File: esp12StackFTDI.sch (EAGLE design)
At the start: 23 parts, among them J02 470, J04 470, J05 470, J12 470, J13 470

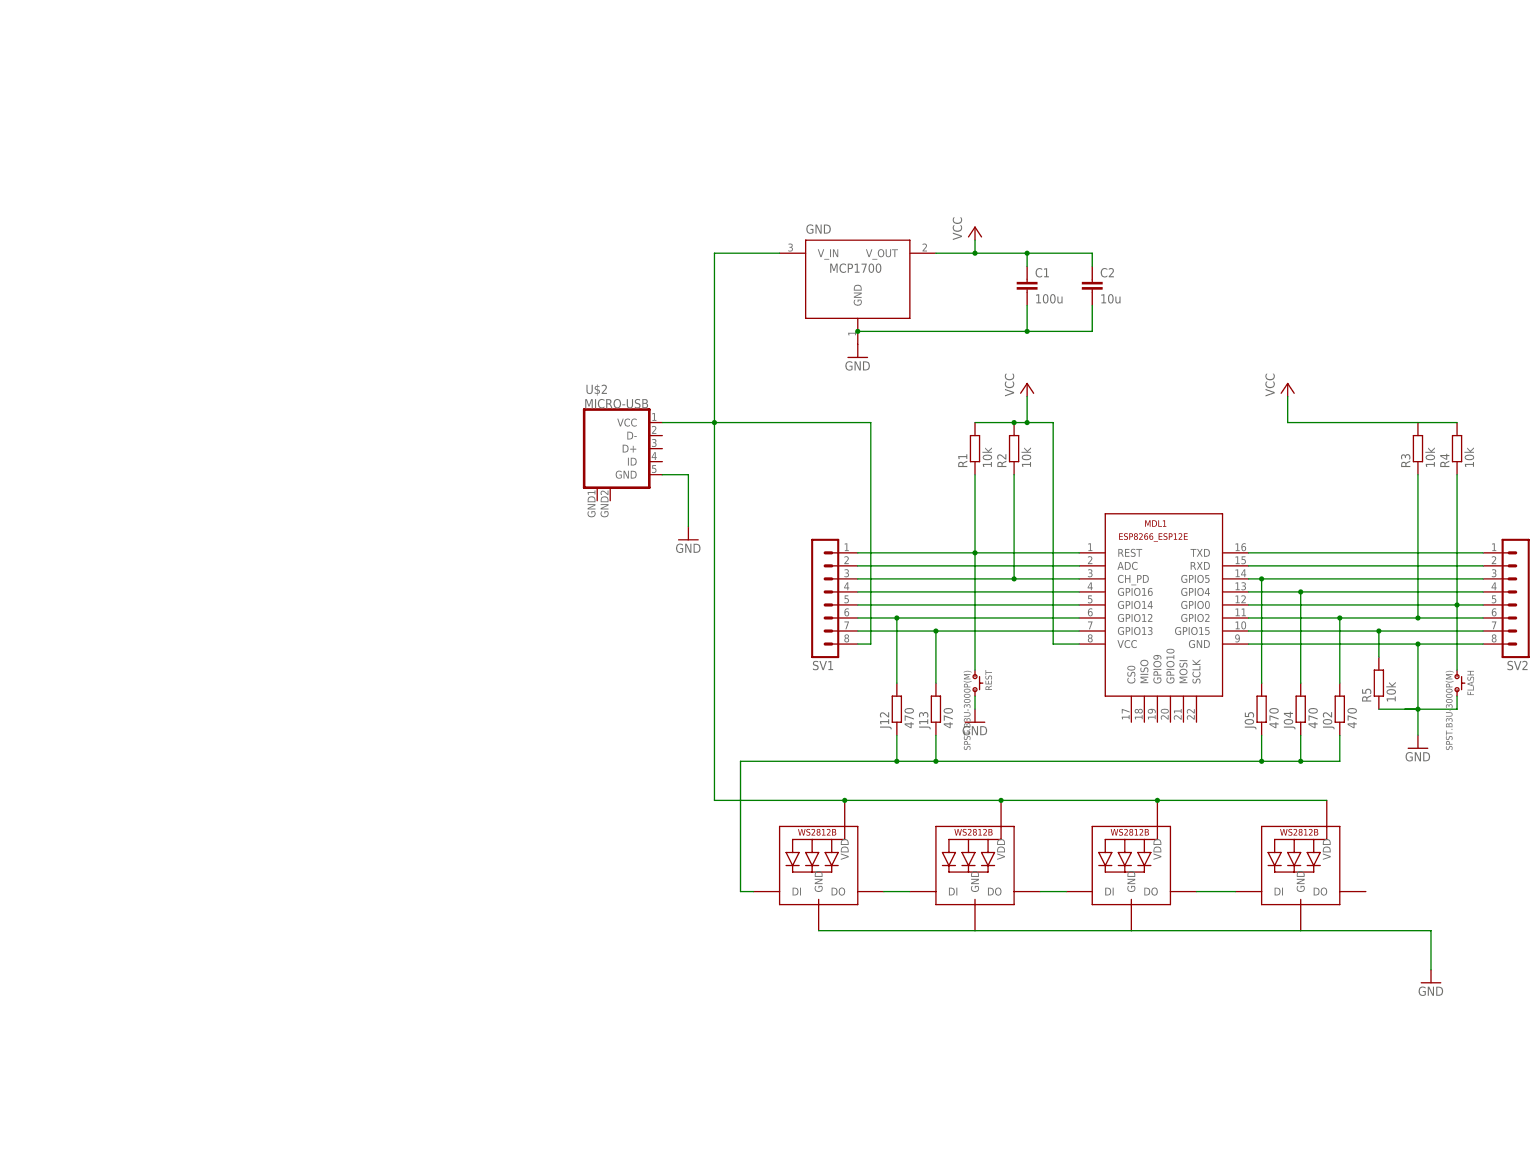
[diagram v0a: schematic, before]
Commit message: added an ftdi version
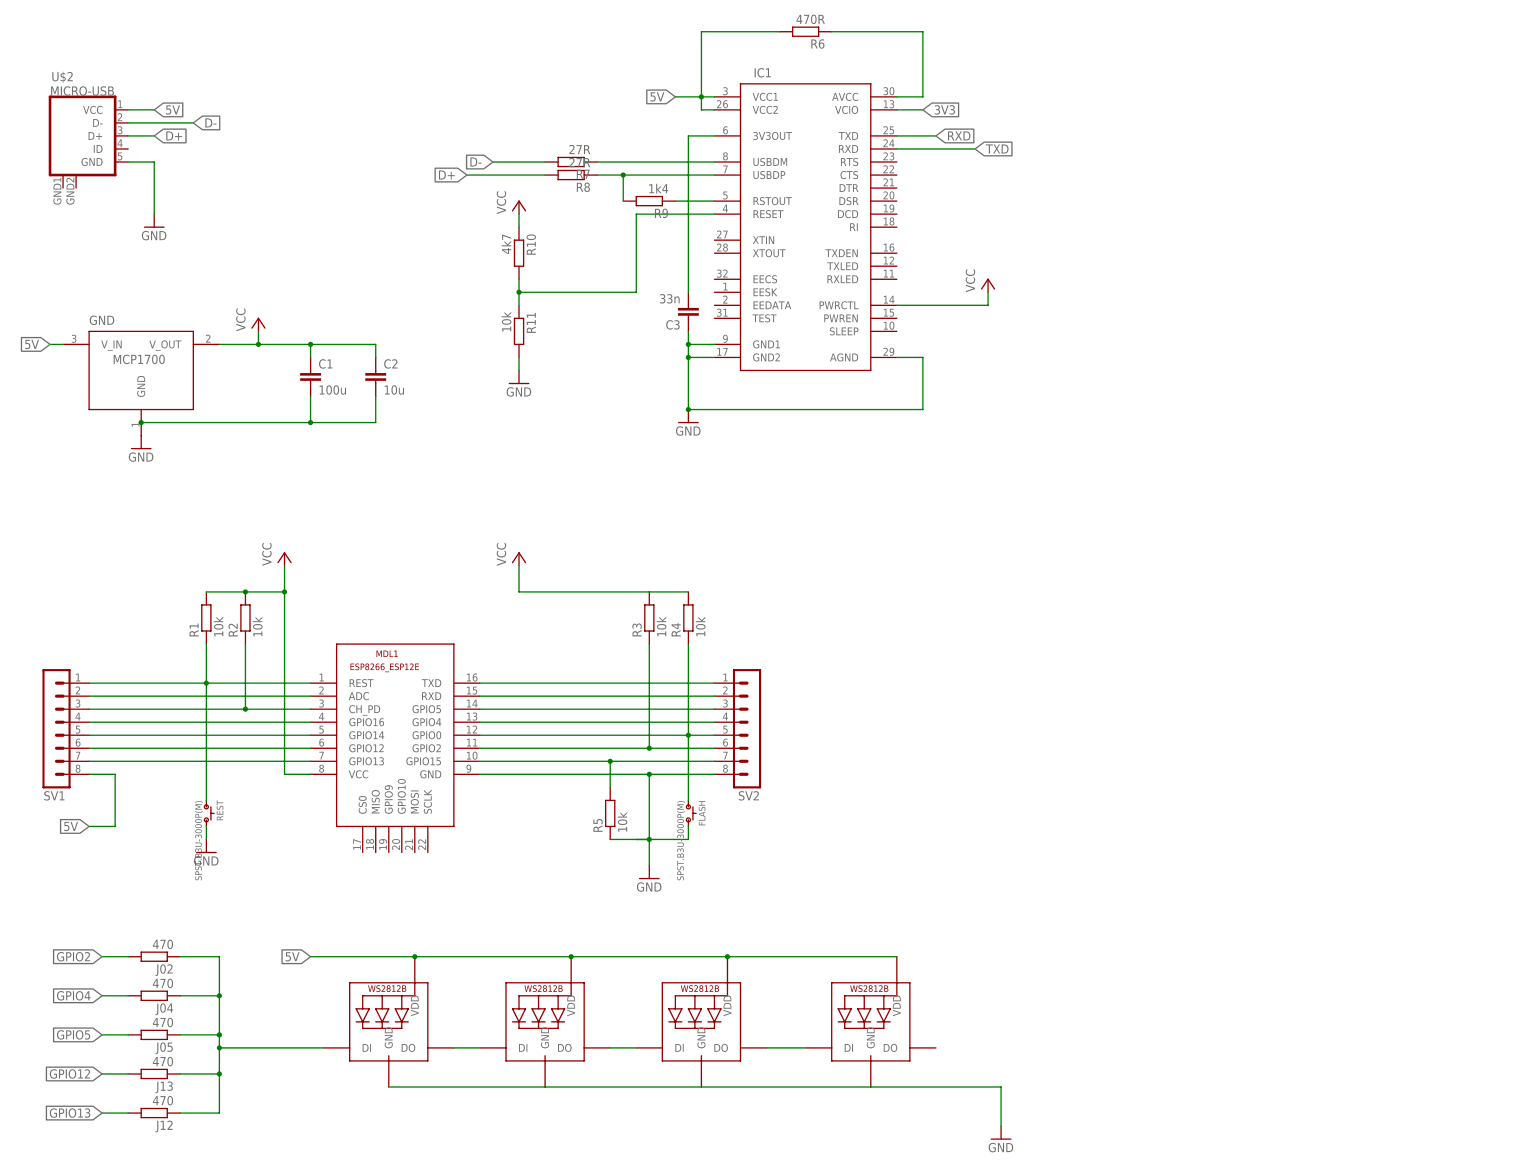
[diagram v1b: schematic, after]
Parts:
- added C3: 33n, eagle-ltspice:CC0603
- added IC1: (no value), FTDI:FT232BM
- added R10: 4k7, eagle-ltspice:RR0603
- added R11: 10k, eagle-ltspice:RR0603
- added R6: 470R, eagle-ltspice:RR0603
- added R7, R8: 27R, eagle-ltspice:RR0603
- added R9: 1k4, eagle-ltspice:RR0603
- J02, J04, J05, J12, J13, R1, R2, R3, R4, R5: device eagle-ltspice:R -> eagle-ltspice:RR0603
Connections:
- net DIN renamed DIN1
- new net 3V3OUT: C3.2, IC1.3V3OUT
- new net AVCC: IC1.AVCC, R6.1
- new net D+: R8.2, U$2.D+
- new net D-: R7.2, U$2.D-
- new net RESET: IC1.RESET, R10.2, R11.1
- new net RSTOUT: IC1.RSTOUT, R9.1
- new net USBDM: IC1.USBDM, R7.1
- new net USBDP: IC1.USBDP, R8.1, R9.2
- net 3V3: now also IC1.PWRCTL, IC1.VCIO
- net 5V: now also IC1.VCC1, IC1.VCC2, R10.1, R6.2
- net GND: now also C3.1, IC1.AGND, IC1.GND1, IC1.GND2, R11.2
- net GPIO12: now also J13.2; no longer J12.2
- net GPIO13: now also J12.2; no longer J13.2
- net RXD: now also IC1.TXD
- net TXD: now also IC1.RXD
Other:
- moved on the sheet: C1, C2, FLASH, GND, J02, J04, J05, J12, J13, MDL1, R1, R2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

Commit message: Deep Sleep capability
added a jumper Position to connect GIPO16 and REST to enable wake up from deep sleep.
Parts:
- added J_REST: 10k, eagle-ltspice:RR0603
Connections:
- net GPIO16: now also J_REST.1
- net REST: now also J_REST.2
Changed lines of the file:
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@@
 <grid distance="0.1" unitdist="inch" unit="inch" style="lines" multiple="1" display="no" altdistance="0.01" altunitdist="inch" altunit="inch"/>
 <layers>
-<layer number="1" name="Top" color="4" fill="1" visible="yes" active="no"/>
-<layer number="16" name="Bottom" color="1" fill="1" visible="yes" active="no"/>
-<layer number="17" name="Pads" color="2" fill="1" visible="yes" active="no"/>
-<layer number="18" name="Vias" color="2" fill="1" visible="yes" active="no"/>
-<layer number="19" name="Unrouted" color="6" fill="1" visible="yes" active="no"/>
-<layer number="20" name="Dimension" color="15" fill="1" visible="yes" active="no"/>
-<layer number="21" name="tPlace" color="7" fill="1" visible="yes" active="no"/>
-<layer number="22" name="bPlace" color="7" fill="1" visible="yes" active="no"/>
-<layer number="23" name="tOrigins" color="15" fill="1" visible="yes" active="no"/>
-<layer number="24" name="bOrigins" color="15" fill="1" visible="yes" active="no"/>
-<layer number="25" name="tNames" color="7" fill="1" visible="yes" active="no"/>
-<layer number="26" name="bNames" color="7" fill="1" visible="yes" active="no"/>
-<layer number="27" name="tValues" color="7" fill="1" visible="yes" active="no"/>
-<layer number="28" name="bValues" color="7" fill="1" visible="yes" active="no"/>
+<layer number="1" name="Top" color="4" fill="1" visible="no" active="no"/>
+<layer number="16" name="Bottom" color="1" fill="1" visible="no" active="no"/>
+<layer number="17" name="Pads" color="2" fill="1" visible="no" active="no"/>
+<layer number="18" name="Vias" color="2" fill="1" visible="no" active="no"/>
+<layer number="19" name="Unrouted" color="6" fill="1" visible="no" active="no"/>
+<layer number="20" name="Dimension" color="15" fill="1" visible="no" active="no"/>
+<layer number="21" name="tPlace" color="7" fill="1" visible="no" active="no"/>
+<layer number="22" name="bPlace" color="7" fill="1" visible="no" active="no"/>
+<layer number="23" name="tOrigins" color="15" fill="1" visible="no" active="no"/>
+<layer number="24" name="bOrigins" color="15" fill="1" visible="no" active="no"/>
+<layer number="25" name="tNames" color="7" fill="1" visible="no" active="no"/>
+<layer number="26" name="bNames" color="7" fill="1" visible="no" active="no"/>
+<layer number="27" name="tValues" color="7" fill="1" visible="no" active="no"/>
+<layer number="28" name="bValues" color="7" fill="1" visible="no" active="no"/>
 <layer number="29" name="tStop" color="7" fill="3" visible="no" active="no"/>
 <layer number="30" name="bStop" color="7" fill="6" visible="no" active="no"/>
@@
 <layer number="35" name="tGlue" color="7" fill="4" visible="no" active="no"/>
 <layer number="36" name="bGlue" color="7" fill="5" visible="no" active="no"/>
-<layer number="37" name="tTest" color="7" fill="1" visible="yes" active="no"/>
-<layer number="38" name="bTest" color="7" fill="1" visible="yes" active="no"/>
+<layer number="37" name="tTest" color="7" fill="1" visible="no" active="no"/>
+<layer number="38" name="bTest" color="7" fill="1" visible="no" active="no"/>
 <layer number="39" name="tKeepout" color="4" fill="11" visible="no" active="no"/>
 <layer number="40" name="bKeepout" color="1" fill="11" visible="no" active="no"/>
@@
 <layer number="44" name="Drills" color="7" fill="1" visible="no" active="no"/>
 <layer number="45" name="Holes" color="7" fill="1" visible="no" active="no"/>
-<layer number="46" name="Milling" color="3" fill="1" visible="yes" active="no"/>
-<layer number="47" name="Measures" color="7" fill="1" visible="yes" active="no"/>
-<layer number="48" name="Document" color="7" fill="1" visible="yes" active="no"/>
-<layer number="49" name="Reference" color="7" fill="1" visible="yes" active="no"/>
-<layer number="50" name="dxf" color="7" fill="1" visible="yes" active="no"/>
-<layer number="51" name="tDocu" color="7" fill="1" visible="yes" active="no"/>
-<layer number="52" name="bDocu" color="7" fill="1" visible="yes" active="no"/>
-<layer number="53" name="tGND_GNDA" color="7" fill="9" visible="yes" active="no"/>
-<layer number="54" name="bGND_GNDA" color="1" fill="9" visible="yes" active="no"/>
-<layer number="56" name="wert" color="7" fill="1" visible="yes" active="no"/>
-<layer number="57" name="tCAD" color="7" fill="1" visible="yes" active="no"/>
-<layer number="59" name="tCarbon" color="7" fill="1" visible="yes" active="no"/>
-<layer number="60" name="bCarbon" color="7" fill="1" visible="yes" active="no"/>
+<layer number="46" name="Milling" color="3" fill="1" visible="no" active="no"/>
+<layer number="47" name="Measures" color="7" fill="1" visible="no" active="no"/>
+<layer number="48" name="Document" color="7" fill="1" visible="no" active="no"/>
+<layer number="49" name="Reference" color="7" fill="1" visible="no" active="no"/>
+<layer number="50" name="dxf" color="7" fill="1" visible="no" active="no"/>
+<layer number="51" name="tDocu" color="7" fill="1" visible="no" active="no"/>
+<layer number="52" name="bDocu" color="7" fill="1" visible="no" active="no"/>
+<layer number="53" name="tGND_GNDA" color="7" fill="9" visible="no" active="no"/>
+<layer number="54" name="bGND_GNDA" color="1" fill="9" visible="no" active="no"/>
+<layer number="56" name="wert" color="7" fill="1" visible="no" active="no"/>
+<layer number="57" name="tCAD" color="7" fill="1" visible="no" active="no"/>
+<layer number="59" name="tCarbon" color="7" fill="1" visible="no" active="no"/>
+<layer number="60" name="bCarbon" color="7" fill="1" visible="no" active="no"/>
 <layer number="90" name="Modules" color="5" fill="1" visible="yes" active="yes"/>
 <layer number="91" name="Nets" color="2" fill="1" visible="yes" active="yes"/>
@@
 <part name="P+2" library="supply1" deviceset="VCC" device=""/>
 <part name="P+5" library="supply1" deviceset="VCC" device=""/>
+<part name="J_REST" library="eagle-ltspice" deviceset="R" device="R0603" value="10k"/>
 </parts>
 <sheets>
@@
 <instance part="P+2" gate="VCC" x="-35.56" y="111.76"/>
 <instance part="P+5" gate="VCC" x="55.88" y="96.52"/>
+<instance part="J_REST" gate="G$1" x="-111.76" y="30.48" rot="R90"/>
 </instances>
 <busses>
@@
 <wire x1="-76.2" y1="17.78" x2="-96.52" y2="17.78" width="0.1524" layer="91"/>
 <pinref part="R1" gate="G$1" pin="1"/>
-<wire x1="-96.52" y1="17.78" x2="-119.38" y2="17.78" width="0.1524" layer="91"/>
+<wire x1="-96.52" y1="17.78" x2="-106.68" y2="17.78" width="0.1524" layer="91"/>
+<wire x1="-106.68" y1="17.78" x2="-119.38" y2="17.78" width="0.1524" layer="91"/>
 <wire x1="-96.52" y1="25.4" x2="-96.52" y2="17.78" width="0.1524" layer="91"/>
 <junction x="-96.52" y="17.78"/>
 <wire x1="-96.52" y1="17.78" x2="-96.52" y2="-5.08" width="0.1524" layer="91"/>
 <pinref part="REST" gate="G$1" pin="1"/>
+<pinref part="J_REST" gate="G$1" pin="2"/>
+<wire x1="-111.76" y1="35.56" x2="-106.68" y2="35.56" width="0.1524" layer="91"/>
+<wire x1="-106.68" y1="35.56" x2="-106.68" y2="17.78" width="0.1524" layer="91"/>
+<junction x="-106.68" y="17.78"/>
 </segment>
 </net>
@@
 <pinref part="MDL1" gate="G$1" pin="GPIO16"/>
 <pinref part="SV1" gate="1" pin="4"/>
-<wire x1="-76.2" y1="10.16" x2="-119.38" y2="10.16" width="0.1524" layer="91"/>
+<wire x1="-76.2" y1="10.16" x2="-111.76" y2="10.16" width="0.1524" layer="91"/>
+<pinref part="J_REST" gate="G$1" pin="1"/>
+<wire x1="-111.76" y1="10.16" x2="-119.38" y2="10.16" width="0.1524" layer="91"/>
+<wire x1="-111.76" y1="10.16" x2="-111.76" y2="25.4" width="0.1524" layer="91"/>
+<junction x="-111.76" y="10.16"/>
 </segment>
 </net>

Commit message: FT232 module
FT232 Module now functional as a prototype
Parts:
- removed C3: 33n, eagle-ltspice:CC0603
- removed IC1: (no value), FTDI:FT232BM
- removed R8: 27R, eagle-ltspice:RR0603
- removed R9: 1k4, eagle-ltspice:RR0603
- added C4: 10nF, eagle-ltspice:C
- added C5: 100nF, eagle-ltspice:C
- added D1: (no value), adafruit:DIODESOD-323F
- added LED5, LED6: (no value), adafruit:LEDCHIPLED_0603
- added SJ2: SOLDERJUMPERNC2, SparkFun:SOLDERJUMPERNC2
- added U1: (no value), ftdichip-4:FT232RL
- R6: value 470R -> (none); device eagle-ltspice:RR0603 -> rcl:R-EU_R0603
- R7: value 27R -> (none); device eagle-ltspice:RR0603 -> rcl:R-EU_R0603
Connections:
- removed net AVCC: IC1.AVCC, R6.1
- removed net RSTOUT: IC1.RSTOUT, R9.1
- removed net USBDM: IC1.USBDM, R7.1
- removed net USBDP: IC1.USBDP, R8.1, R9.2
- new net 5VUSB: D1.A, U$2.VCC
- new net CBUS3: R6.2, U1.CBUS3
- new net CBUS4: R7.1, U1.CBUS4
- new net LED_RX: LED6.C, R7.2
- new net LED_TX: LED5.C, R6.1
- net 3V3: now also LED5.A, LED6.A, U1.VCCIO; no longer IC1.PWRCTL, IC1.VCIO
- net 3V3OUT: now also C5.2, U1.3V3OUT; no longer C3.2, IC1.3V3OUT
- net 5V: now also C4.2, D1.C, U1.VCC; no longer IC1.VCC1, IC1.VCC2, R6.2, U$2.VCC
- net D+: now also U1.USBDP; no longer R8.2
- net D-: now also U1.USBDM; no longer R7.2
- net DIN1: now also SJ2.2
- net GND: now also C4.1, C5.1, U1.AGND, U1.GND1, U1.GND2, U1.GND3, U1.TEST; no longer C3.1, IC1.AGND, IC1.GND1, IC1.GND2
- net GPIO2: now also SJ2.1
- net RESET: now also U1.RESET#; no longer IC1.RESET
- net RXD: now also U1.TXD; no longer IC1.TXD
- net TXD: now also U1.RXD; no longer IC1.RXD
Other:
- moved on the sheet: C1, C2, R10, R11, R6, R7
